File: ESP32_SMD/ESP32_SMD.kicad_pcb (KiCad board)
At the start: 2 copper layers, 100 x 100 mm, 25 parts, among them J1 Conn_01x02_Socket, J10 Conn_01x02_Socket, J11 Conn_01x15_Socket, J12 Conn_01x02_Socket, J13 Conn_01x02_Socket, J14 Conn_01x02_Socket, J15 Conn_01x02_Socket, J16 Conn_01x02_Socket, J2 Conn_01x02_Socket, J3 Serial Converter, J4 I2C, J5 Conn_01x02_Socket, J6 Conn_01x02_Socket, J7 Conn_01x02_Socket, J8 Conn_01x02_Socket, J9 Conn_01x02_Socket, SW1 SW_Nidec_CAS-120A1, SW2 SW_DPST_x2, SW3 SW_DPST_x2, U1 ESP32-WROOM-32E

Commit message: v1.0.1
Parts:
- SW1: footprint Connector_PinHeader_2.54mm:PinHeader_1x03_P2.54mm_Vertical -> TerminalBlock:TerminalBlock_Xinya_XY308-2.54-3P_1x03_P2.54mm_Horizontal
- moved SW3 20.0 mm to (83.8, 107.8), turned to 180 degrees
- moved C1 12.8 mm to (81.5, 97.0)
- moved C2 12.8 mm to (66.5, 97.5), turned to 180 degrees
- moved SW2 7.77 mm to (70.8, 107.8), turned to 180 degrees
- moved SW1 3.81 mm to (36.5, 107.0), turned to 0 degrees
- moved J5 1.62 mm to (16.0, 78.2), turned to 90 degrees
- moved J11 0.57 mm to (24.2, 21.5)
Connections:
- C1 pad 2: Net-(J11-Pin_1) -> Net-(J11-Pin_11)
- J12 pad 1: Net-(J11-Pin_3) -> Net-(J11-Pin_10)
- J12 pad 2: Net-(J11-Pin_1) -> Net-(J11-Pin_11)
- J13 pad 1: Net-(J11-Pin_7) -> Net-(J11-Pin_15)
- J13 pad 2: Net-(J11-Pin_6) -> Net-(J11-Pin_14)
- J14 pad 1: Net-(J11-Pin_11) -> Net-(J11-Pin_4)
- J14 pad 2: Net-(J11-Pin_10) -> Net-(J11-Pin_3)
- J15 pad 1: Net-(J11-Pin_13) -> Net-(J11-Pin_5)
- J16 pad 1: Net-(J11-Pin_15) -> Net-(J11-Pin_8)
- J16 pad 2: Net-(J11-Pin_14) -> Net-(J11-Pin_13)
- J2 pad 1: Net-(J11-Pin_2) -> Net-(J11-Pin_7)
- J2 pad 2: Net-(J11-Pin_4) -> Net-(J11-Pin_6)
- J3 pad 3: Net-(J11-Pin_2) -> Net-(J11-Pin_7)
- J3 pad 4: Net-(J11-Pin_4) -> Net-(J11-Pin_6)
- J5 pad 1: Net-(J11-Pin_5) -> Net-(J11-Pin_2)
- J5 pad 2: Net-(J11-Pin_8) -> Net-(J11-Pin_9)
- J6 pad 1: Net-(J11-Pin_9) -> Net-(J11-Pin_1)
- SW3 pad 2: Net-(J11-Pin_1) -> Net-(J11-Pin_11)
- U1 pad 13: Net-(J11-Pin_9) -> Net-(J11-Pin_1)
- U1 pad 14: Net-(J11-Pin_7) -> Net-(J11-Pin_15)
- U1 pad 16: Net-(J11-Pin_8) -> Net-(J11-Pin_2)
- U1 pad 23: Net-(J11-Pin_10) -> Net-(J11-Pin_3)
- U1 pad 24: Net-(J11-Pin_3) -> Net-(J11-Pin_10)
- U1 pad 25: Net-(J11-Pin_1) -> Net-(J11-Pin_11)
- U1 pad 26: Net-(J11-Pin_5) -> Net-(J11-Pin_9)
- U1 pad 27: Net-(J11-Pin_11) -> Net-(J11-Pin_4)
- U1 pad 29: Net-(J11-Pin_6) -> Net-(J11-Pin_14)
- U1 pad 30: Net-(J11-Pin_13) -> Net-(J11-Pin_5)
- U1 pad 31: Net-(J11-Pin_14) -> Net-(J11-Pin_13)
- U1 pad 34: Net-(J11-Pin_4) -> Net-(J11-Pin_6)
- U1 pad 35: Net-(J11-Pin_2) -> Net-(J11-Pin_7)
- U1 pad 37: Net-(J11-Pin_15) -> Net-(J11-Pin_8)
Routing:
- net Net-(J11-Pin_6): track 55.8 -> 169.6 mm
- net Net-(J11-Pin_7): track 65.3 -> 172.6 mm
- net Net-(J11-Pin_13): track 35.5 -> 140.3 mm
- net Net-(J11-Pin_11): track 48.3 -> 138.0 mm, vias 0 -> 2
- net Net-(J11-Pin_10): track 46.3 -> 126.1 mm, vias 0 -> 1
- net Net-(J11-Pin_3): track 39.4 -> 116.4 mm, vias 0 -> 1
- net Net-(J11-Pin_9): track 47.3 -> 123.2 mm
- net Net-(J11-Pin_8): track 46.3 -> 113.8 mm
- net Net-(J11-Pin_12): track 35.5 -> 102.1 mm, vias 0 -> 1
- net Net-(J11-Pin_15): track 42.8 -> 105.2 mm
- net Net-(J3-Pin_1): track 63.8 -> 116.7 mm, vias 0 -> 1
- net Net-(J11-Pin_14): track 59.6 -> 101.5 mm
- net Net-(J11-Pin_5): track 58.8 -> 97.4 mm, vias 0 -> 1
- net Net-(J11-Pin_4): track 84.2 -> 116.8 mm, vias 0 -> 1
- net Net-(J11-Pin_2): track 90.9 -> 117.6 mm
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- added copper zone on B.Cu, net GND
- added copper zone on F.Cu, net GND

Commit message: v1.0.0
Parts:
- added J17: I2C, Connector_JST:JST_XH_B2B-XH-A_1x02_P2.50mm_Vertical, F.Cu at (98.0, 49.5)
- added REF**: hole_M3, 00a:hole_M3, F.Cu at (17.0, 107.0)
- added REF**: hole_M3, 00a:hole_M3, F.Cu at (107.0, 17.0)
- added REF**: hole_M3, 00a:hole_M3, F.Cu at (107.0, 107.0)
- added REF**: hole_M3, 00a:hole_M3, F.Cu at (17.0, 17.0)
- moved J11 9.50 mm to (24.2, 31.0)
- moved J9 2.69 mm to (60.5, 17.0), turned to 0 degrees
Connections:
- U1 pad 4: Net-(J9-Pin_2) -> Net-(J9-Pin_1)
- U1 pad 5: Net-(J9-Pin_1) -> Net-(J9-Pin_2)
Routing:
- net Net-(J11-Pin_2): track 117.6 -> 98.6 mm
- net Net-(J11-Pin_4): track 116.8 -> 107.3 mm
- net Net-(J11-Pin_3): track 116.4 -> 106.9 mm
- net Net-(J11-Pin_15): track 105.2 -> 114.7 mm
- net Net-(J11-Pin_14): track 101.5 -> 111.0 mm
- net Net-(J11-Pin_1): track 92.1 -> 82.6 mm
- net Net-(J11-Pin_9): track 123.2 -> 114.0 mm
- net Net-(J17-Pin_1): track 48.3 -> 57.3 mm
- net Net-(J11-Pin_12): track 102.1 -> 94.4 mm
- net Net-(SW2A-B): track 52.4 -> 58.9 mm
- net Net-(J11-Pin_5): track 97.4 -> 92.2 mm
- net Net-(J11-Pin_13): track 140.3 -> 136.2 mm
- net Net-(J11-Pin_8): track 113.8 -> 109.9 mm
- net Net-(J11-Pin_7): track 172.6 -> 168.6 mm
- net Net-(J11-Pin_6): track 169.6 -> 165.7 mm
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
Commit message: v1.0.0
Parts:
- added G***: LOGO, 00a:nuron, F.Cu at (38.7, 85.2)
- added G***: LOGO, 00a:MARC_rogo, F.Cu at (25.0, 86.0)
- added J18: Conn_01x03_Socket, Connector_JST:JST_XH_B3B-XH-A_1x03_P2.50mm_Vertical, F.Cu at (97.0, 17.5)
- added J19: Conn_01x03_Socket, Connector_JST:JST_XH_B3B-XH-A_1x03_P2.50mm_Vertical, F.Cu at (97.0, 30.0)
- moved J3 8.02 mm to (92.0, 100.2), turned to 0 degrees
- moved J12 2.69 mm to (108.0, 76.0), turned to -90 degrees
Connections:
- J12 pad 1: Net-(J11-Pin_10) -> Net-(J11-Pin_11)
- J12 pad 2: Net-(J11-Pin_11) -> Net-(J11-Pin_10)
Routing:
- net Net-(J11-Pin_11): track 135.0 -> 202.9 mm
- net Net-(J11-Pin_4): track 107.3 -> 173.3 mm
- net Net-(J11-Pin_5): track 92.2 -> 147.6 mm
- net Net-(J11-Pin_12): track 94.4 -> 143.7 mm
- net Net-(J11-Pin_15): track 114.7 -> 134.4 mm
- net Net-(J11-Pin_14): track 111.0 -> 123.7 mm
- net Net-(J11-Pin_6): track 165.7 -> 174.6 mm
- net Net-(J3-Pin_1): track 116.7 -> 121.5 mm
- net Net-(J11-Pin_7): track 168.6 -> 170.3 mm
- net Net-(J11-Pin_10): track 124.1 -> 125.2 mm
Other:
- board text added: "+"
- board text added: "+5V"
- board text added: "-"
- board text added: "0"
- board text added: "1"
- board text added: "12"
- board text added: "13"
- board text added: "14"
- board text added: "15"
- board text added: "16"
- board text added: "17"
- board text added: "18"
- board text added: "19"
- board text added: "2"
- board text added: "23"
- board text added: "25"
- board text added: "26"
- board text added: "27"
- board text added: "3"
- board text added: "32"
- board text added: "33"
- board text added: "34"
- board text added: "35"
- board text added: "36"
- board text added: "39"
- board text added: "4"
- board text added: "5"
- board text added: "BOOT"
- board text added: "ESP32_SMD_v1.0.0"
- board text added: "GND"
- board text added: "OFF"
- board text added: "ON"
- board text added: "RESET"
- board text added: "RxD"
- board text added: "SCL"
- board text added: "SDA"
- board text added: "TxD"

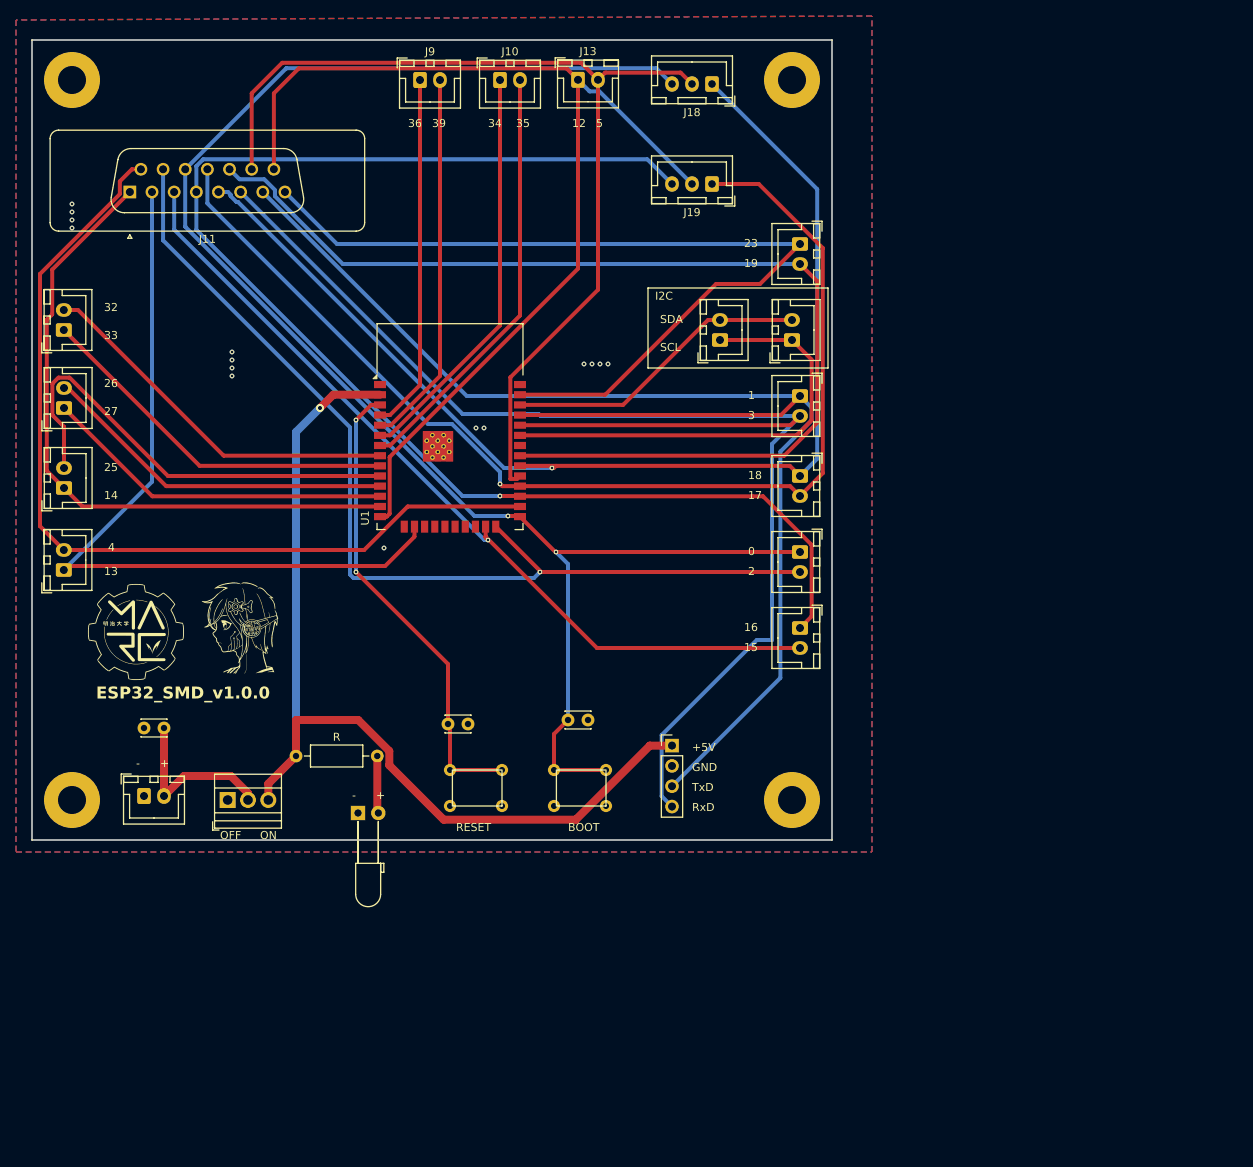
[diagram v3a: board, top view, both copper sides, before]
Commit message: v1.1.0
・3端子レギュレータを追加
・ポリスイッチを追加
・配線を改良
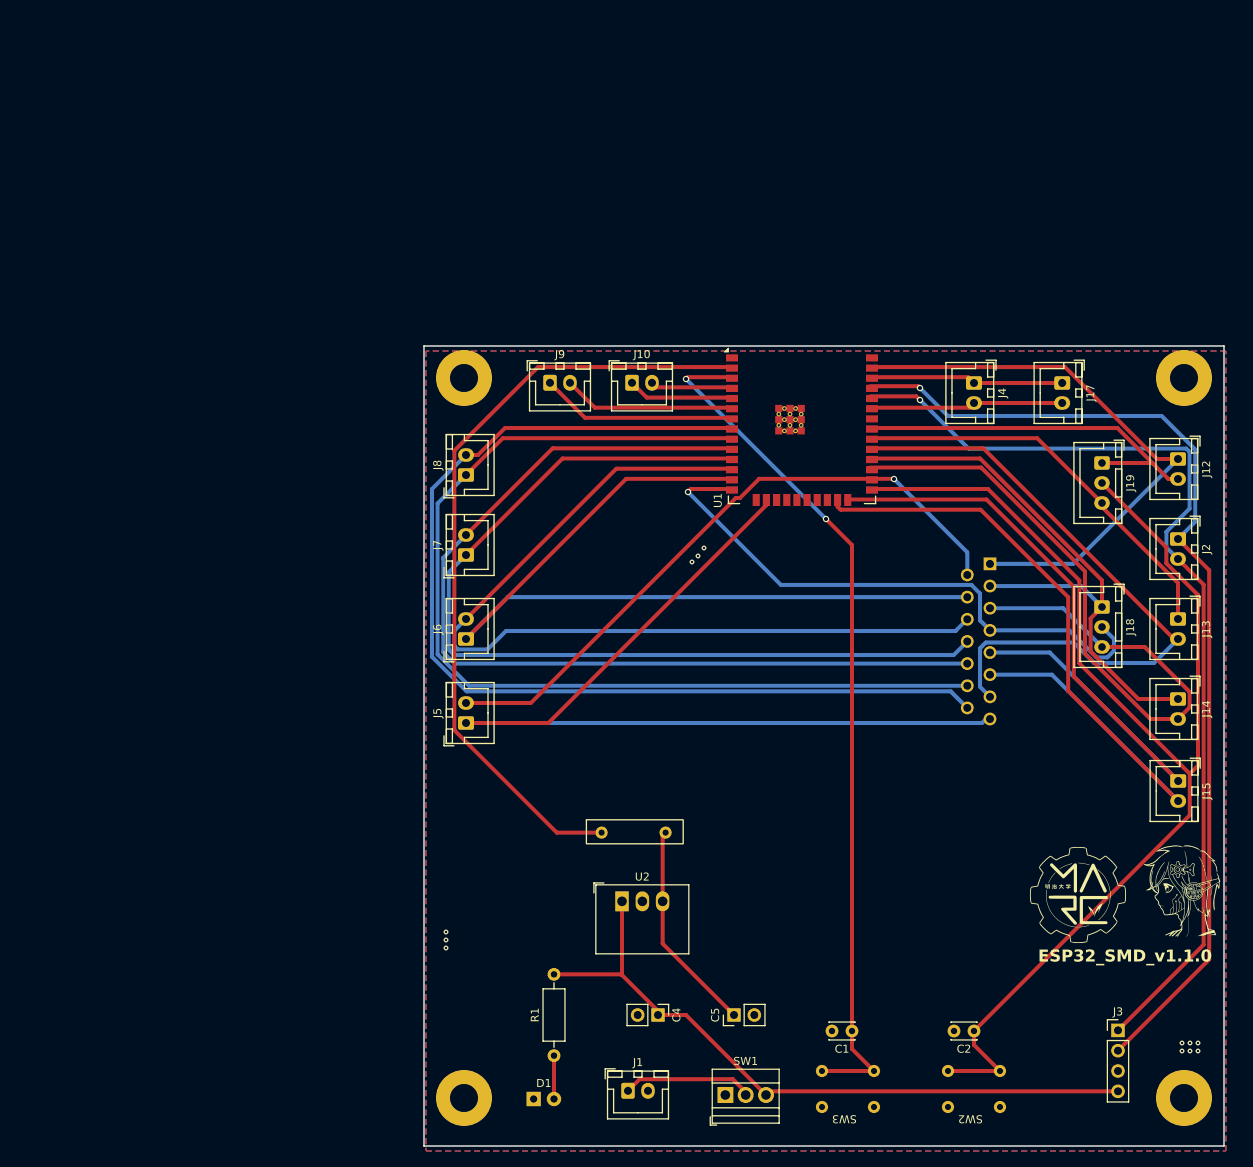
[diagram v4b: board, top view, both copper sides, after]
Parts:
- removed C3: 22uF, Capacitor_THT:C_Disc_D3.0mm_W2.0mm_P2.50mm
- removed J16: Conn_01x02_Socket, Connector_JST:JST_XH_B2B-XH-A_1x02_P2.50mm_Vertical
- added C4: C, Connector_PinHeader_2.54mm:PinHeader_1x02_P2.54mm_Vertical, F.Cu at (90.2, 133.9)
- added C5: C, Connector_PinHeader_2.54mm:PinHeader_1x02_P2.54mm_Vertical, F.Cu at (99.8, 133.9)
- added F1: Polyfuse, 00a:RXEF005, F.Cu at (81.3, 109.5)
- added U2: R-78B1.2-2.0, Converter_DCDC:Converter_DCDC_RECOM_R-78B-2.0_THT, F.Cu at (85.8, 119.7)
- J1: value Conn_01x02_Socket -> POWER
- J10: value Conn_01x02_Socket -> INPUT_2
- J11: moved to B.Cu
- J9: value Conn_01x02_Socket -> INPUT_1
- SW2, SW3: footprint 00b:DTS-63 -> 00a:DTS-63-N-V
- U1: footprint RF_Module:ESP32-WROOM-32D -> 00a:ESP32-WROOM-32E
- moved G*** 122.3 mm to (156.4, 118.1)
- moved G*** 122.3 mm to (142.8, 118.9)
- moved J11 117.1 mm to (131.8, 77.5), turned to 90 degrees
- moved J13 100.8 mm to (155.2, 84.4), turned to -90 degrees
- moved J18 81.6 mm to (145.8, 82.9), turned to -90 degrees
- moved C2 74.0 mm to (129.8, 135.9)
- moved SW2 72.7 mm to (133.0, 145.4)
- moved SW1 72.3 mm to (98.7, 143.9)
- moved J1 70.8 mm to (86.5, 143.3)
- moved J3 66.1 mm to (147.8, 135.8)
- moved REF** 61.6 mm to (66.0, 144.2)
- moved REF** 61.6 mm to (156.0, 54.2)
- moved REF** 61.6 mm to (156.0, 144.2)
- moved REF** 61.6 mm to (66.0, 54.2)
- moved J15 60.7 mm to (155.3, 104.6)
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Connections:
- net Net-(J11-Pin_9) renamed IO4
- C1 pad 1: GND -> Net-(SW3A-B)
- C1 pad 2: Net-(J11-Pin_11) -> GND
- C2 pad 1: GND -> IO0
- C2 pad 2: Net-(SW2A-B) -> GND
- J1 pad 1: GND -> Net-(J1-Pin_1)
- J1 pad 2: Net-(J1-Pin_2) -> GND
- J11 pad 1: Net-(J11-Pin_1) -> IO23
- J11 pad 10: Net-(J11-Pin_10) -> IO14
- J11 pad 11: Net-(J11-Pin_11) -> IO27
- J11 pad 12: Net-(J11-Pin_12) -> IO26
- J11 pad 13: Net-(J11-Pin_13) -> IO25
- J11 pad 14: Net-(J11-Pin_14) -> IO33
- J11 pad 15: Net-(J11-Pin_15) -> IO32
- J11 pad 2: Net-(J11-Pin_2) -> IO17
- J11 pad 3: Net-(J11-Pin_3) -> IO16
- J11 pad 4: Net-(J11-Pin_4) -> IO12
- J11 pad 5: Net-(J11-Pin_5) -> IO2
- J11 pad 6: Net-(J11-Pin_6) -> IO15
- J11 pad 7: Net-(J11-Pin_7) -> IO5
- J11 pad 8: Net-(J11-Pin_8) -> IO13
- J12 pad 1: Net-(J11-Pin_11) -> IO23
- J12 pad 2: Net-(J11-Pin_10) -> IO19
- J13 pad 1: Net-(J11-Pin_15) -> IO18
- J13 pad 2: Net-(J11-Pin_14) -> IO5
- J14 pad 1: Net-(J11-Pin_4) -> IO17
- J14 pad 2: Net-(J11-Pin_3) -> IO16
- J15 pad 1: Net-(J11-Pin_5) -> IO2
- J15 pad 2: Net-(J11-Pin_12) -> IO15
- J18 pad 1: Net-(J11-Pin_5) -> IO17
- J18 pad 2: Net-(J11-Pin_14) -> IO12
- J18 pad 3: Net-(J11-Pin_11) -> IO16
- J19 pad 1: Net-(J11-Pin_12) -> IO19
- J19 pad 2: Net-(J11-Pin_15) -> IO0
- J19 pad 3: Net-(J11-Pin_4) -> IO18
- J2 pad 1: Net-(J11-Pin_7) -> IO1
- J2 pad 2: Net-(J11-Pin_6) -> IO3
- J3 pad 1: Net-(J3-Pin_1) -> IO3
- J3 pad 2: GND -> IO1
- J3 pad 3: Net-(J11-Pin_7) -> GND
- J3 pad 4: Net-(J11-Pin_6) -> Net-(J3-Pin_4)
- J5 pad 1: Net-(J11-Pin_2) -> IO13
- J6 pad 1: Net-(J11-Pin_1) -> IO14
- J6 pad 2: Net-(J6-Pin_2) -> IO27
- J7 pad 1: Net-(J7-Pin_1) -> IO26
- J7 pad 2: Net-(J7-Pin_2) -> IO25
- J8 pad 1: Net-(J8-Pin_1) -> IO33
- J8 pad 2: Net-(J8-Pin_2) -> IO32
- R1 pad 2: Net-(J3-Pin_1) -> Net-(J3-Pin_4)
- SW1 pad 2: Net-(J1-Pin_2) -> Net-(J1-Pin_1)
- SW1 pad 3: Net-(J3-Pin_1) -> Net-(J3-Pin_4)
- SW2 pad 2: Net-(SW2A-B) -> IO0
- SW3 pad 2: Net-(J11-Pin_11) -> Net-(SW3A-B)
- U1 pad 10: Net-(J6-Pin_2) -> IO25
- U1 pad 11: Net-(J7-Pin_2) -> IO26
- U1 pad 12: Net-(J7-Pin_1) -> IO27
- U1 pad 13: Net-(J11-Pin_1) -> IO14
- U1 pad 14: Net-(J11-Pin_15) -> IO12
- U1 pad 16: Net-(J11-Pin_2) -> IO13
- U1 pad 2: Net-(J3-Pin_1) -> Net-(U1-VDD)
- U1 pad 23: Net-(J11-Pin_3) -> IO15
- U1 pad 24: Net-(J11-Pin_10) -> IO2
- U1 pad 25: Net-(J11-Pin_11) -> IO0
- U1 pad 27: Net-(J11-Pin_4) -> IO16
- U1 pad 28: Net-(J11-Pin_12) -> IO17
- U1 pad 29: Net-(J11-Pin_14) -> IO5
- U1 pad 3: Net-(SW2A-B) -> Net-(SW3A-B)
- U1 pad 30: Net-(J11-Pin_5) -> IO18
- U1 pad 31: Net-(J11-Pin_13) -> IO19
- U1 pad 33: Net-(J17-Pin_1) -> Net-(J17-Pin_2)
- U1 pad 34: Net-(J11-Pin_6) -> IO3
- U1 pad 35: Net-(J11-Pin_7) -> IO1
- U1 pad 36: Net-(J17-Pin_2) -> Net-(J17-Pin_1)
- U1 pad 37: Net-(J11-Pin_8) -> IO23
- U1 pad 4: Net-(J9-Pin_1) -> Net-(J10-Pin_2)
- U1 pad 5: Net-(J9-Pin_2) -> Net-(J10-Pin_1)
- U1 pad 6: Net-(J10-Pin_1) -> Net-(J9-Pin_2)
- U1 pad 7: Net-(J10-Pin_2) -> Net-(J9-Pin_1)
- U1 pad 8: Net-(J8-Pin_2) -> IO32
- U1 pad 9: Net-(J8-Pin_1) -> IO33
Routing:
- net Net-(J11-Pin_11): track 202.9 -> 0.00 mm, vias 2 -> 0
- net Net-(J11-Pin_6): track 174.6 -> 0.00 mm
- net Net-(J11-Pin_4): track 173.3 -> 0.00 mm, vias 1 -> 0
- net Net-(J11-Pin_7): track 170.3 -> 0.00 mm
- net IO0: track 0.00 -> 159.0 mm
- net Net-(J11-Pin_5): track 147.6 -> 0.00 mm, vias 1 -> 0
- net Net-(J11-Pin_12): track 143.7 -> 0.00 mm, vias 1 -> 0
- net Net-(J11-Pin_13): track 136.2 -> 0.00 mm
- net Net-(J11-Pin_15): track 134.4 -> 0.00 mm
- net IO32: track 0.00 -> 130.7 mm
- net IO33: track 0.00 -> 126.4 mm
- net IO1: track 0.00 -> 126.3 mm, vias 0 -> 1
- net Net-(J11-Pin_10): track 125.2 -> 0.00 mm, vias 1 -> 0
- net Net-(J11-Pin_14): track 123.7 -> 0.00 mm
- net IO3: track 0.00 -> 122.7 mm, vias 0 -> 1
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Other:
- board text added: "ESP32_SMD_v1.1.0"
- board text removed: "+"
- board text removed: "+5V"
- board text removed: "-"
- board text removed: "0"
- board text removed: "1"
- board text removed: "12"
- board text removed: "13"
- board text removed: "14"
- board text removed: "15"
- board text removed: "16"
- board text removed: "17"
- board text removed: "18"
- board text removed: "19"
- board text removed: "2"
- board text removed: "23"
- board text removed: "25"
- board text removed: "26"
- board text removed: "27"
- board text removed: "3"
- board text removed: "32"
- board text removed: "33"
- board text removed: "34"
- board text removed: "35"
- board text removed: "36"
- board text removed: "39"
- board text removed: "4"
- board text removed: "5"
- board text removed: "BOOT"
- board text removed: "ESP32_SMD_v1.0.0"
- board text removed: "GND"
- board text removed: "OFF"
- board text removed: "ON"
- board text removed: "RESET"
- board text removed: "RxD"
- board text removed: "SCL"
- board text removed: "SDA"
- board text removed: "TxD"

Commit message: 2024/10/15
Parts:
- added R2: 10kΩ, Resistor_THT:R_Axial_DIN0207_L6.3mm_D2.5mm_P10.16mm_Horizontal, F.Cu at (83.2, 106.0)
- R1: value R -> 240Ω
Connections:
- J3 pad 1: IO3 -> IO1
- J3 pad 2: IO1 -> IO3
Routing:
- net Net-(SW3A-B): track 108.1 -> 129.3 mm
- net Net-(U1-VDD): track 97.2 -> 102.3 mm
- net IO3: track 122.7 -> 126.3 mm
- net IO1: track 126.3 -> 125.2 mm
